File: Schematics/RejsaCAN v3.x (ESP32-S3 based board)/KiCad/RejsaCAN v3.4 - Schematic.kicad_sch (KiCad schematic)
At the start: 83 parts, among them J1 Micro-Fit 3.0 4P R/A, J2 U.FL, J3 JST-XH 4P LTE, Q1 SS8050, U1 ESP32-S3-WROOM-1(N16R8), U2 SN65HVD230DR, U3 ME2807A33M3G, U4 LMR51610XDBVR, U5 MT9700, U6 GAQY212GS, U7 LG290P03AAMD, U8 AP2112K-3.3

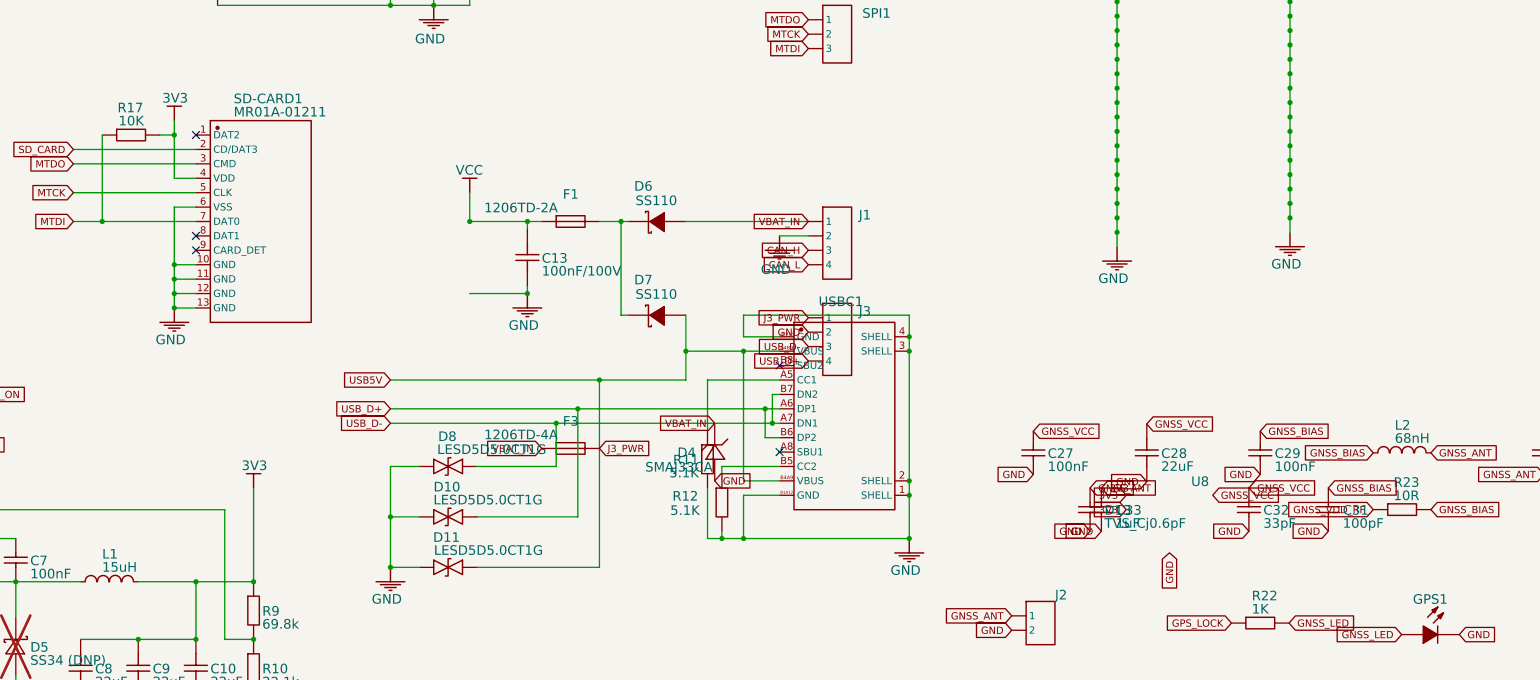
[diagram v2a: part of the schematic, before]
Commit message: BOM: verified, stocked LCSC part on every line; equivalents for the unstocked ones
Every symbol now carries Manufacturer Part / Manufacturer / Supplier Part
(LCSC C-number) checked against LCSC stock on 2026-08-18. Land patterns of
the substitutes were compared numerically (EasyEDA footprint API) where the
package mattered:

- SD-CARD1: ATOM MR01A-01211 (C479742, out of stock) -> SOFNG TF-015
  (C113206): identical TF-015-family land within 0.1 mm incl. the two 1.0 mm
  pegs; XYECONN/SHOU HAN clones put the pegs 0.35 mm further out.
- L1: no 15 uH with adequate Isat in the SLP6028S land at LCSC -> the
  upstream SLP6028S100MTT 10 uH (C254862, 2.2 A, 35 mR, exact land).
- L2: 68 nH LQW15AN out of stock -> LQW15AN47NJ00D 47 nH wirewound
  (C192855, 228k); the ferrite-core 68 nH parts (SRF 750-800 MHz) are
  useless at L1/L5.
- U8: AP2112K-3.3 has 5 pcs -> RT9013-33GB (C47773, same SOT-23-5 pinout,
  low noise/high PSRR).
- D6/D7: SS110 in SOD-123F only exists as SMAF at LCSC -> onsemi
  MBR1H100SFT3G SOD-123FL 100 V 1 A (C235757).
- D13: 0.5 pF ESD9L5.0ST5G (C82326); its SOD-923 pads sit inside the 0402 land.
- F1 0466002.NRHF 2 A/63 V fast (C3105); F3 Walter 1206T4A63V 4 A time-lag
  (C354899). C6 CL32B225KCJSNNE (C55151), C13 CL10B104KC8NNNC (C15725),
  D4 MDD SMAJ33CA (C115251), U4 C20539658, U6 AQY212GS C719745, J1 C122413,
  J2 U.FL-R-SMT-1(10) C88373 (the field used to hold a pin-header C-number),
  J3 B4B-XH-A C144395.
- U7 LG290P03AAMD: not at LCSC (DigiKey ~$71-81), field says so.

The stale copied fields (D13 = a Samsung capacitor, F1/F3 = the old 1812
PTC, U4 = LMR14006, C6/C13 wrong dielectrics) would have matched wrong parts
in a JLC BOM upload. PCB Value fields re-synced; DRC unchanged (0 errors).

Co-Authored-By: Claude Fable 5 <noreply@anthropic.com>
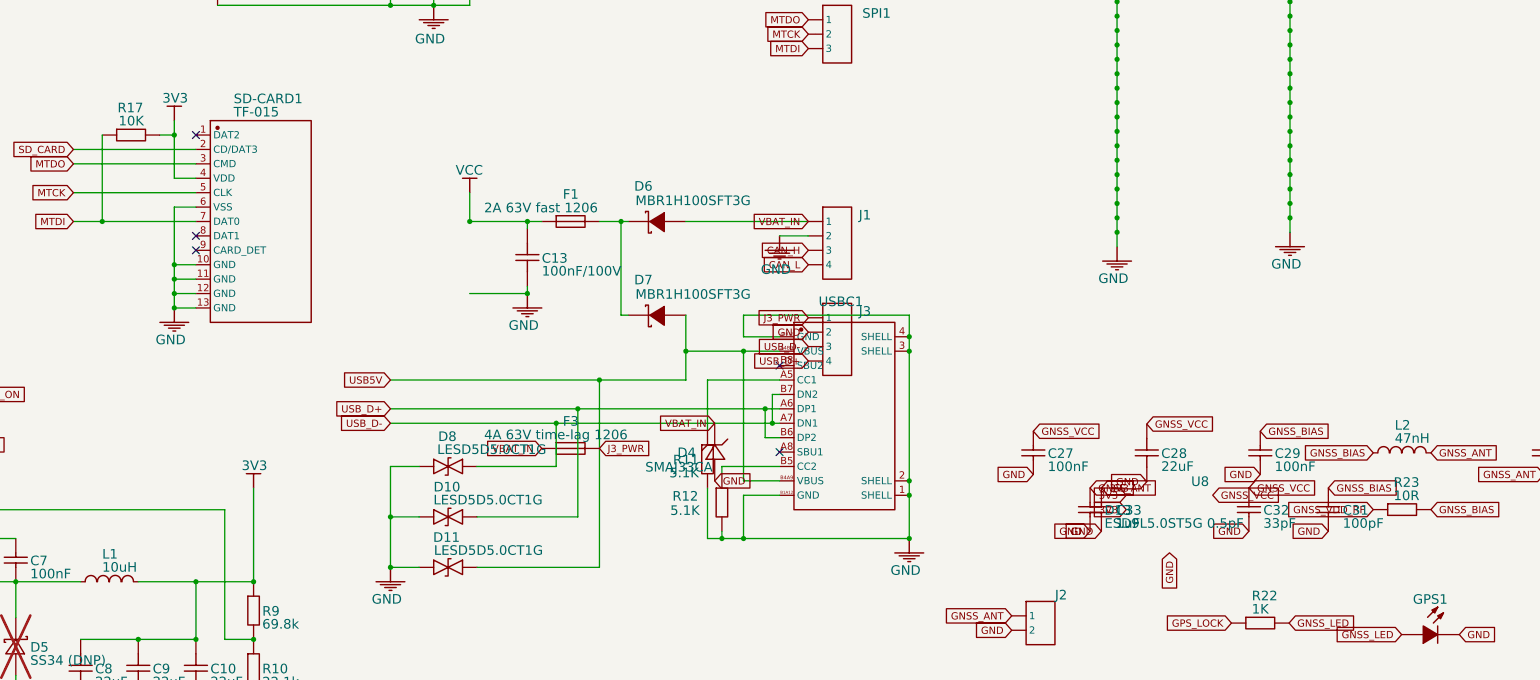
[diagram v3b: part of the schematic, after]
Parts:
- C10, C11, C12, C2, C27, C28, C29, C3, C4, C5, C7, C8, C9: Manufacturer SAMSUNG -> Samsung Electro-Mechanics
- C13: Manufacturer Part CL05B104KB54PNC -> CL10B104KC8NNNC; Supplier Part (none) -> C15725
- C30: Manufacturer SAMSUNG -> FH; Manufacturer Part CL05B104KO5NNNC -> 0402CG101J500NT; Supplier Part C1525 -> C1546
- C31: Manufacturer SAMSUNG -> FH; Manufacturer Part CL05B104KO5NNNC -> 0402CG101J500NT; Supplier Part (none) -> C1546
- C32: Manufacturer SAMSUNG -> FH; Manufacturer Part CL05B104KO5NNNC -> 0402CG330J500NT; Supplier Part (none) -> C1562
- C33: Manufacturer SAMSUNG -> Samsung Electro-Mechanics; Manufacturer Part CL05B104KO5NNNC -> CL05A105KA5NQNC; Supplier Part (none) -> C52923
- C6: Manufacturer Part CL21A226MAYNNNE -> CL32B225KCJSNNE; Supplier Part (none) -> C55151
- D1, D2, D3, D9: Manufacturer Part 1N4148WS T4 -> 1N4148WS
- D13: value TVS_Cj0.6pF -> ESD9L5.0ST5G 0.5pF; Manufacturer SAMSUNG -> onsemi; Manufacturer Part CL05B104KO5NNNC -> ESD9L5.0ST5G; Supplier Part (none) -> C82326
- D4: Manufacturer DOWO -> MDD; Manufacturer Part SMF30A -> SMAJ33CA; Supplier Part (none) -> C115251
- D6, D7: value SS110 -> MBR1H100SFT3G; Manufacturer STARSEA -> onsemi; Manufacturer Part DSS34 -> MBR1H100SFT3G; Supplier Part (none) -> C235757
- F1: value 1206TD-2A -> 2A 63V fast 1206; Manufacturer BOURNS -> Littelfuse; Manufacturer Part MF-MSMF110/16-2 -> 0466002.NRHF; Supplier Part (none) -> C3105
- F3: value 1206TD-4A -> 4A 63V time-lag 1206; Manufacturer BOURNS -> Walter Elec; Manufacturer Part MF-MSMF110/16-2 -> 1206T4A63V; Supplier Part (none) -> C354899
- GPIO1, I2C1: Manufacturer (none) -> Ckmtw; Manufacturer Part (none) -> B-2100S04P-A110
- J1: Manufacturer (none) -> Molex; Manufacturer Part (none) -> 43045-0400; Supplier Part (none) -> C122413
- J2: Manufacturer (none) -> Hirose; Manufacturer Part (none) -> U.FL-R-SMT-1(10); Supplier Part C124378 -> C88373
- J3: Manufacturer (none) -> JST; Manufacturer Part (none) -> B4B-XH-A(LF)(SN); Supplier Part (none) -> C144395
- JUMPER1: Manufacturer Part (none) -> DNP
- L1: value 15uH -> 10uH; Supplier Part (none) -> C254862
- L2: value 68nH -> 47nH; Manufacturer Sunltech Tech -> Murata; Manufacturer Part SLP6028S100MTT -> LQW15AN47NJ00D; Supplier Part C254862 -> C192855
- R10: Manufacturer Part 0402WGF1002TCE -> 0402WGF2212TCE; Supplier LCSC -> (none)
- R20: Manufacturer Part 0402WGF4700TCE -> 0402WGF3900TCE; Supplier LCSC -> (none)
- R23: Manufacturer Part 0402WGF1001TCE -> 0402WGF100JTCE; Supplier Part (none) -> C25077
- R9: Manufacturer Part 0402WGF3302TCE -> 0402WGF6982TCE; Supplier LCSC -> (none)
- SD-CARD1: value MR01A-01211 -> TF-015; Manufacturer ATOM(爱特姆) -> SOFNG; Manufacturer Part MR01A-01211 -> TF-015; Supplier Part C479742 -> C113206
- SPI1: Manufacturer Part (none) -> 2.54mm 1x3 header; Supplier LCSC -> (none); Supplier Part C180248 -> (none)
- U1: Manufacturer ESPRESSIF(乐鑫) -> Espressif; Manufacturer Part ESP32-S3-WROOM-1(N16R8) -> ESP32-S3-WROOM-1-N16R8
- U2: Manufacturer TI -> Texas Instruments
- U3: Manufacturer Nanjing Micro One Elec -> Micro One
- U4: Manufacturer Part LMR14006XDDCR -> LMR51610XDBVR; Supplier Part (none) -> C20539658
- U6: value GAQY212GS -> AQY212GS; Manufacturer (none) -> Panasonic; Manufacturer Part (none) -> AQY212GS; Supplier Part (none) -> C719745
- U7: Manufacturer (none) -> Quectel; Manufacturer Part (none) -> LG290P03AAMD; Supplier LCSC -> DigiKey
- U8: value AP2112K-3.3 -> RT9013-33GB; Manufacturer (none) -> RICHTEK; Manufacturer Part (none) -> RT9013-33GB; Supplier Part (none) -> C47773
- USBC1: Manufacturer G-Switch(品赞) -> G-Switch
